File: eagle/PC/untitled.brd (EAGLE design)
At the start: 160 x 100 mm, 4 parts

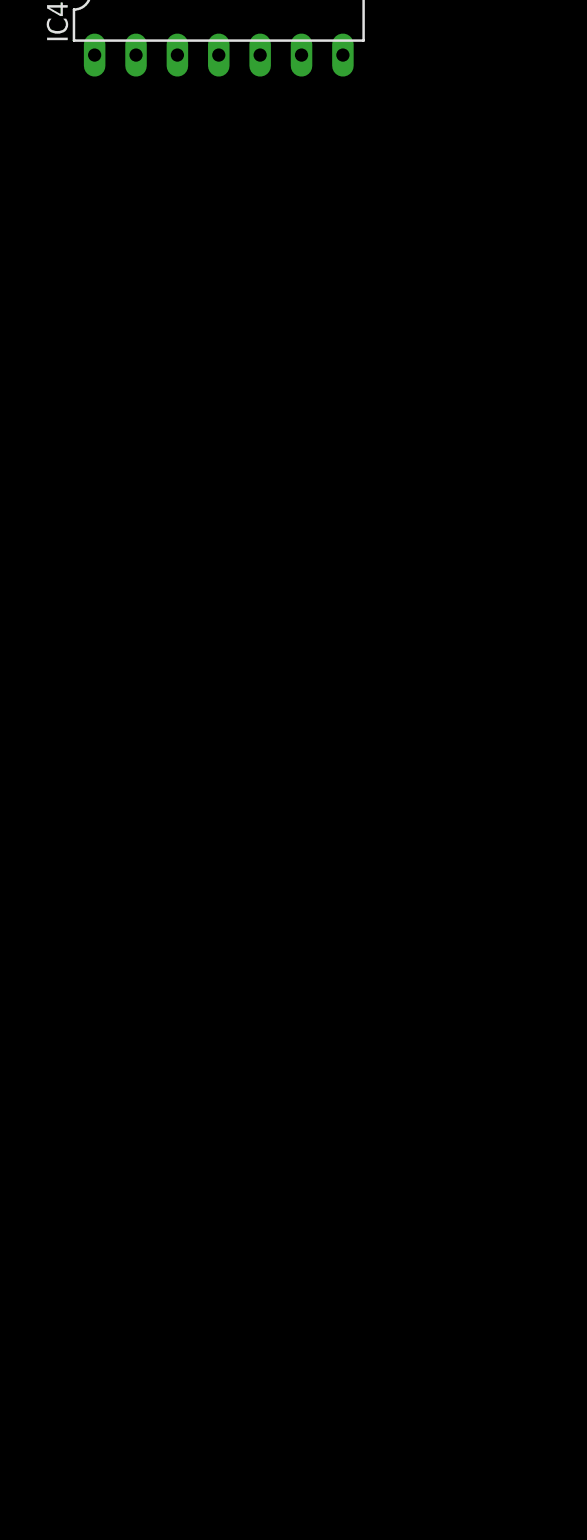
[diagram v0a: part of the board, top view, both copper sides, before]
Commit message: Added first version of Program Counter.
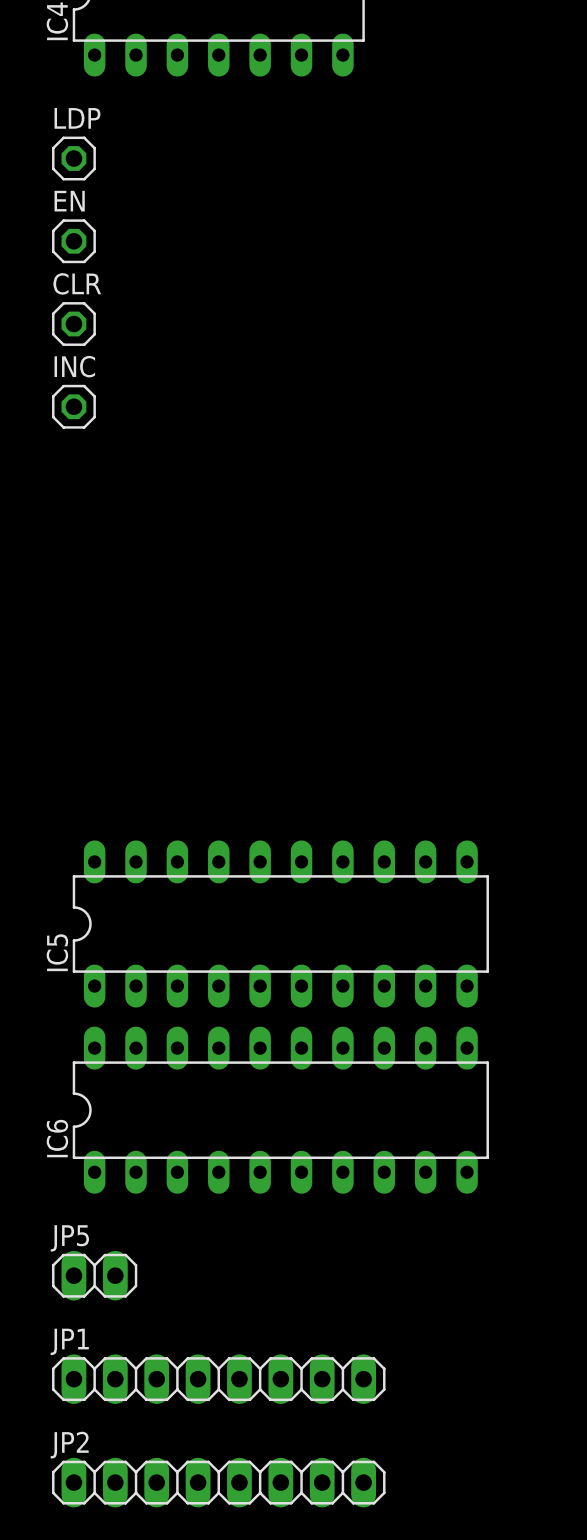
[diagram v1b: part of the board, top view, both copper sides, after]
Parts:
- added CLR, EN, INC, LDP: (no value), pinhead:1X01
- added IC5, IC6: (no value), ic-package:DIL20
- added JP1, JP2: (no value), pinhead:1X08
- added JP5: (no value), pinhead:1X02
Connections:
- new net EN: EN.1, IC5.19, IC6.19
- new net N$1: IC1.1, IC2.1, IC3.1, IC4.1, LDP.1
- new net N$2: CLR.1, IC1.13, IC2.13, IC3.13, IC4.13
- new net N$3: IC1.8, INC.1
- new net P0: IC1.4, IC5.2, JP1.1
- new net P1: IC1.10, IC5.3, JP1.2
- new net P10: IC3.3, IC6.4, JP2.3
- new net P11: IC3.11, IC6.5, JP2.4
- new net P12: IC4.4, IC6.6, JP2.5
- new net P13: IC4.10, IC6.7, JP2.6
- new net P14: IC4.3, IC6.8, JP2.7
- new net P15: IC4.11, IC6.9, JP2.8
- new net P2: IC1.3, IC5.4, JP1.3
- new net P3: IC1.11, IC5.5, JP1.4
- new net P4: IC2.4, IC5.6, JP1.5
- new net P5: IC2.10, IC5.7, JP1.6
- new net P6: IC2.3, IC5.8, JP1.7
- new net P7: IC2.11, IC5.9, JP1.8
- new net P8: IC3.4, IC6.2, JP2.1
- new net P9: IC3.10, IC6.3, JP2.2
- new net Q0: IC1.5, IC1.6, IC5.18
- new net Q1: IC1.9, IC5.17
- new net Q10: IC3.2, IC6.16
- new net Q11: IC3.12, IC4.8, IC6.15
- new net Q12: IC4.5, IC4.6, IC6.14
- new net Q13: IC4.9, IC6.13
- new net Q14: IC4.2, IC6.12
- new net Q15: IC4.12, IC6.11
- new net Q2: IC1.2, IC5.16
- new net Q3: IC1.12, IC2.8, IC5.15
- new net Q4: IC2.5, IC2.6, IC5.14
- new net Q5: IC2.9, IC5.13
- new net Q6: IC2.2, IC5.12
- new net Q7: IC2.12, IC3.8, IC5.11
- new net Q8: IC3.5, IC3.6, IC6.18
- new net Q9: IC3.9, IC6.17
- net GND: now also IC5.1, IC5.10, IC6.1, IC6.10, JP5.2
- net VCC: now also IC5.20, IC6.20, JP5.1
